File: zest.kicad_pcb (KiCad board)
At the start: 8 copper layers, 110 x 181.8 mm, 447 parts, among them J1001 142-0701-201, J1002 U.FL-R-SMT(10), J1003 U.FL-R-SMT(10), J1004 142-0701-201, J1005 U.FL-R-SMT(10), J1201 142-0701-201, J1202 142-0701-201, J1401 ASP-134604-01, J1402 ASP-134604-01, J1501 10029449-111RLF, J1502 PPPC072LJBN-RC, J1503 PPPC072LJBN-RC, J1901 961102-6404-AR, J201 142-0701-201, J202 142-0701-201, J203 142-0701-201, J204 142-0701-201, J701 142-0701-201, J702 142-0701-201, J703 142-0701-201, J704 142-0701-201, J801 20pin 50mil Header, J802 20pin 50mil Header, J901 U.FL-R-SMT(10), J902 U.FL-R-SMT(10), J903 U.FL-R-SMT(10), J904 U.FL-R-SMT(10), J905 U.FL-R-SMT(10), J906 U.FL-R-SMT(10), Q1501 FDN335N, Q1502 FDN335N, T1001 TCM2-43X+, T1002 TCM2-43X+, U1001 TCP-2-33W+, U1002 LMK01801BISQE/NOPB, U1101 AD7794BRUZ, U1201 AD9781BCPZ, U1301 AMC7823IRTAT, U1601 LT6233CS6#TRMPBF, U1701 SN74LVC8T245PWR, U1702 SN74LVC8T245PWR, U1703 SN74LVC8T245PWR, U1704 SN74AVC4T245PWR, U1705 SN74AVC4T245PWR, U1801 ADL5501AKSZ-R7, U1901 AT24C64D-SSHM-T, U2001 KX023-1025-FR, U201 AD9653BCPZ-125, U2701 TPS62110RSAR, U2801 LTC6655CHLS8-2.5#PBF, U2901 TPS62110RSAR, U3001 LT6233CS6#TRMPBF, U3002 PBSS4230T,215, U3101 LT1763IDE-3.3#PBF, U3201 LT1763IDE-1.8#PBF, U701 AD9653BCPZ-125, U901 BAT54W-7-F, U902 ZXCT1009QFTA, U903 LT6233CS6#TRMPBF

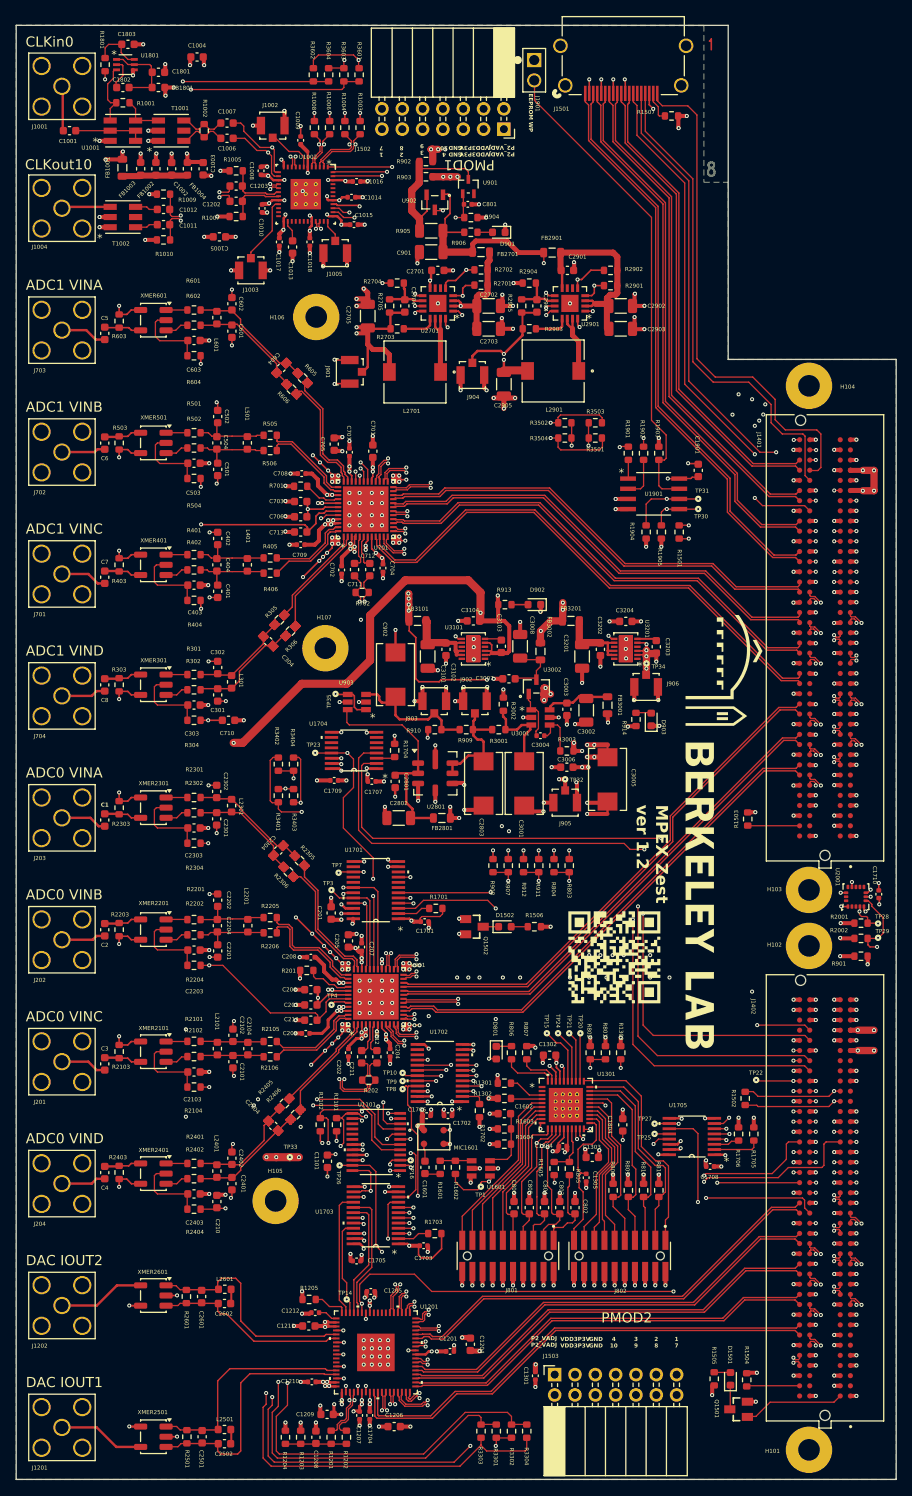
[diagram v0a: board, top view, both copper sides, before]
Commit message: Further Project cleanup
-Added BOM and fabrication files
-updated all documentation files
- Added suggested DC blocking cap at DAC outputs

-Set DRC to 5mil trace and space and fixed various violations detailed below
- Removed various small tracks overlapping IC pads on U2701,U2901,U3101,U3201
- Spaced vias 5 mil apart around U701, U201, 1201
- Moved LMK_CLKout3 pair on In4 layer away from PMOD1_1 pin
- adjusted track into pin47 on U701 to clear pin 48
- adjusted trace under U903 to give more room from ground pads/vias
- spaced out vias around pins45/46 of U201

-Many tweak to trace to go through the center of pad throughout the design
-An example is the trace around C3005
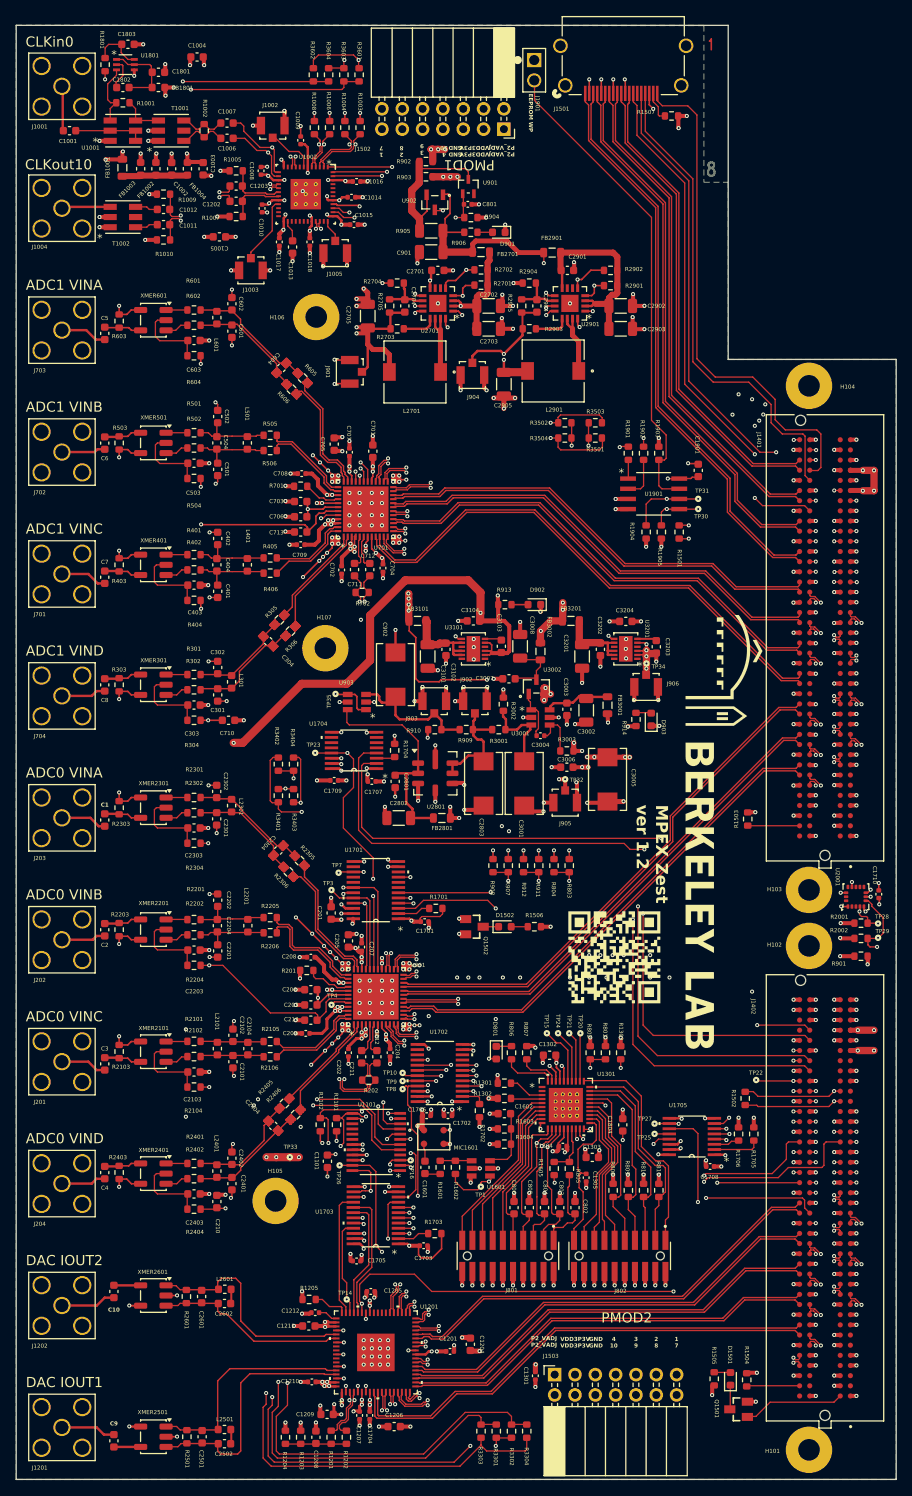
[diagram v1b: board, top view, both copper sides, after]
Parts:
- added C10: 10nF, Capacitor_SMD:C_0603_1608Metric, F.Cu at (159.9, 203.5)
- added C9: 10nF, Capacitor_SMD:C_0603_1608Metric, F.Cu at (159.9, 222.1)
- J1001, J1004, J1201, J1202, J201, J202, J203, J204, J701, J702, J703, J704: value 142-0701-201 -> SMA
- XMER2501, XMER2601: value TC4-6+ -> TC4-6T+
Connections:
- J1201 pad 1: /ad9781/diff2se_0/SE+ -> Net-(J1201-In)
- J1202 pad 1: /ad9781/diff2se_1/SE- -> Net-(J1202-In)
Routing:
- net GND: track 1026.3 -> 645.7 mm
- net /ad9781/diff2se_1/SE-: track 10.9 -> 3.35 mm
- net /ad9781/diff2se_0/SE+: track 10.9 -> 3.37 mm
- net Net-(J1202-In): track 0.00 -> 6.90 mm
- net Net-(J1201-In): track 0.00 -> 6.87 mm
- net /VSS1P8V: track 144.5 -> 146.1 mm
- net /P1_12PV0: track 98.7 -> 99.6 mm
- net Net-(U3101-IN): track 10.4 -> 11.1 mm
- net /VSS3P3V: track 146.1 -> 146.7 mm
